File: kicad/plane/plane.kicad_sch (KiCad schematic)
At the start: 25 parts, among them J1 Battery, M1 Left_Aileron_Servo, M2 Right_Aileron_Servo, M3 Elevator_Servo, M4 Rudder_Servo, U1 LD1085V50, U10 ADS1115, U11 GY - GPS6MV2, U2 ESC, U3 LD1085V50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

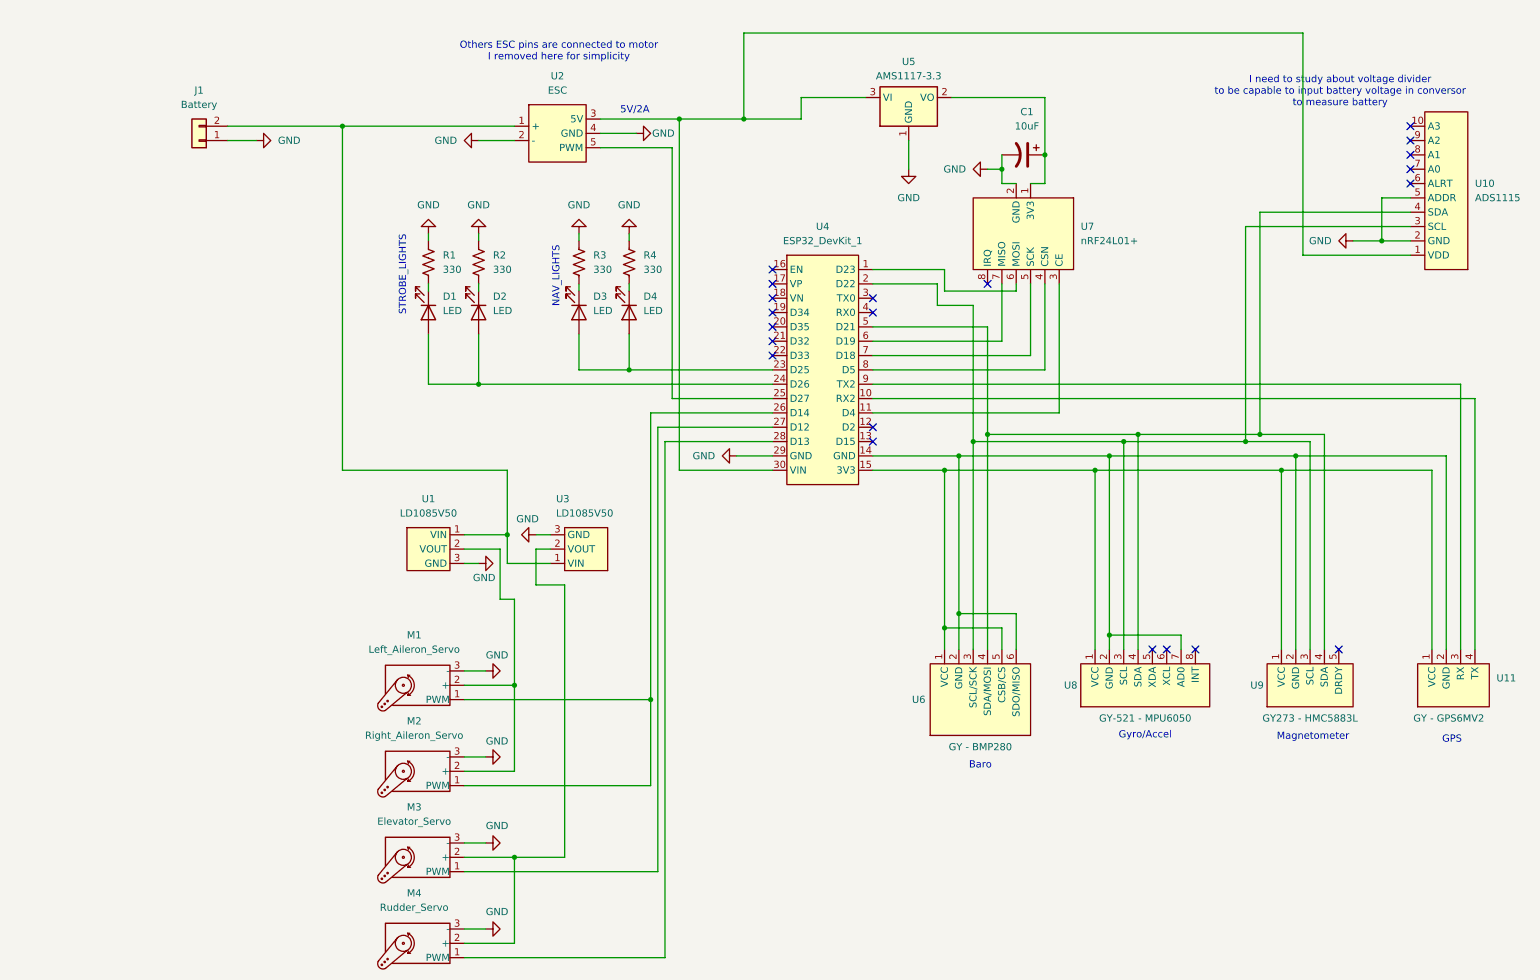
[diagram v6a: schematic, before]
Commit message: pcb without sensors (just rc) is ready to production hehehe
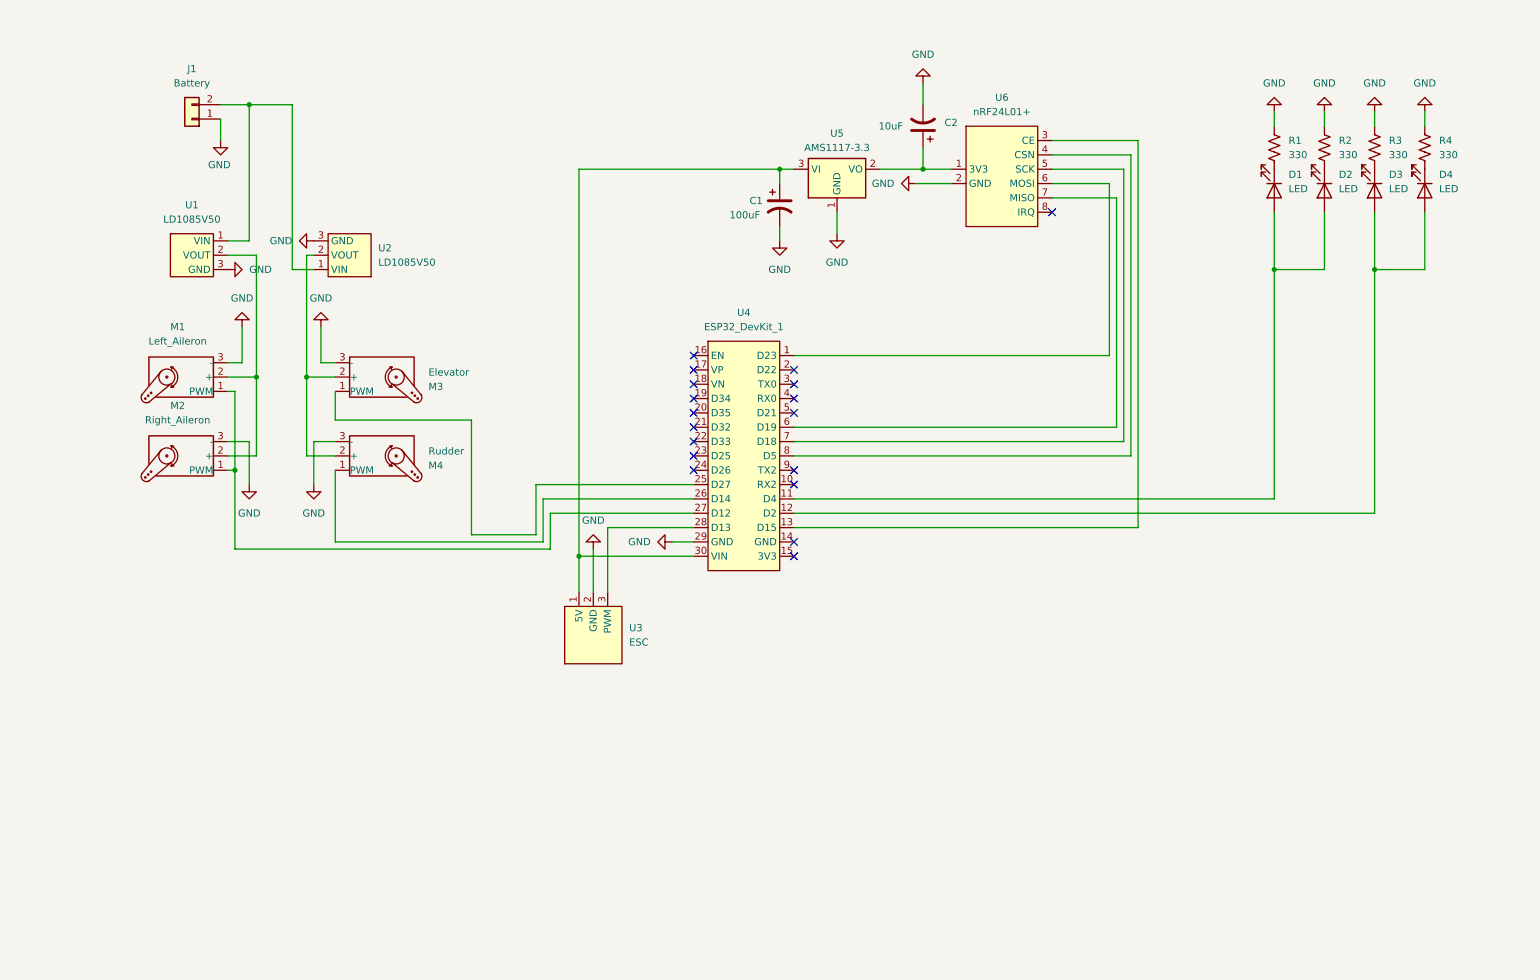
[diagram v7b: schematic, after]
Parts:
- removed U10: ADS1115, PlaneFootprints:ADS1115, symbol PlaneComponents:ADS1115
- removed U11: GY - GPS6MV2, PlaneFootprints:GPS6MV2, symbol PlaneComponents:GY_-_GPS6MV2
- removed U2: ESC, PlaneFootprints:ESC, symbol PlaneComponents:ESC
- removed U3: LD1085V50, PlaneFootprints:LD1085V50, symbol PlaneComponents:LD1085V50
- removed U6: GY - BMP280, PlaneFootprints:BMP280, symbol PlaneComponents:GY - BMP280
- removed U7: nRF24L01+, PlaneFootprints:nRF24L01+, symbol PlaneComponents:nRF24L01+
- removed U8: GY-521 - MPU6050, PlaneFootprints:MPU6050, symbol PlaneComponents:GY-521 - MPU6050
- removed U9: GY273 - HMC5883L, PlaneFootprints:HMC5883L, symbol PlaneComponents:GY273 - HMC5883L
- added C2: 10uF, Capacitor_THT:CP_Radial_D8.0mm_P2.50mm, symbol Device:C_Polarized_US
- added U2: LD1085V50, PlaneFootprints:LD1085V50, symbol PlaneComponents:LD1085V50
- added U3: ESC, Connector_PinHeader_2.54mm:PinHeader_1x03_P2.54mm_Vertical, symbol PlaneComponents:ESC
- added U6: nRF24L01+, PlaneFootprints:nRF24L01+, symbol PlaneComponents:nRF24L01+
- C1: value 10uF -> 100uF
- D1, D2, D3, D4: footprint PlaneFootprints:LED -> Connector_PinHeader_2.54mm:PinHeader_1x02_P2.54mm_Vertical
- M1: value Left_Aileron_Servo -> Left_Aileron
- M2: value Right_Aileron_Servo -> Right_Aileron
- M3: value Elevator_Servo -> Elevator
- M4: value Rudder_Servo -> Rudder
- R1, R2, R3, R4: footprint Resistor_THT:R_Axial_DIN0207_L6.3mm_D2.5mm_P7.62mm_Horizontal -> Resistor_THT:R_Axial_DIN0207_L6.3mm_D2.5mm_P10.16mm_Horizontal
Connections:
- net GND: now also C2.2, U2.3 (GND), U3.2 (GND), U6.2 (GND)
- net at D3.2 (A), D4.2 (A): now also U4.12 (D2); no longer U4.23 (D25)
- net at J1.2 (Pin_2), U1.1 (VIN): now also U2.1 (VIN)
- net at M3.2 (+), M4.2 (+): now also U2.2 (VOUT)
- net at U4.1 (D23): now also U6.6 (MOSI)
- net at U4.11 (D4): now also D1.2 (A), D2.2 (A)
- net at U4.13 (D15): now also U6.3 (CE)
- net at U4.25 (D27): now also M3.1 (PWM)
- net at M1.1 (PWM), M2.1 (PWM): now also U4.27 (D12); no longer U4.26 (D14)
- net at M4.1 (PWM): now also U4.26 (D14); no longer U4.28 (D13)
- net at U4.30 (VIN), U5.3 (VI): now also C1.1, U3.1 (5V)
- net at U4.6 (D19): now also U6.7 (MISO)
- net at U4.7 (D18): now also U6.5 (SCK)
- net at U4.8 (D5): now also U6.4 (CSN)
- net at U5.2 (VO): now also C2.1, U6.1 (3V3); no longer C1.1
- new net: U3.3 (PWM), U4.28 (D13)
- now unconnected: U4.24 (D26)
- no-connect marks 21 -> 18
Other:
- note removed: "5V/2A"
- note removed: "Baro"
- note removed: "GPS"
- note removed: "Gyro/Accel"
- note removed: "I need to study about voltage divider to be capable to input battery voltage in conversor to measure battery"
- note removed: "Magnetometer"
- note removed: "NAV_LIGHTS"
- note removed: "Others ESC pins are connected to motor I removed here for simplicity"
- note removed: "STROBE_LIGHTS"
